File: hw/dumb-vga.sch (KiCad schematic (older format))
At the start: 17 parts, among them IC1 74HC590N, IC2 74HC590N, IC3 74HC590N, U1 A29040C, X1 VGAF

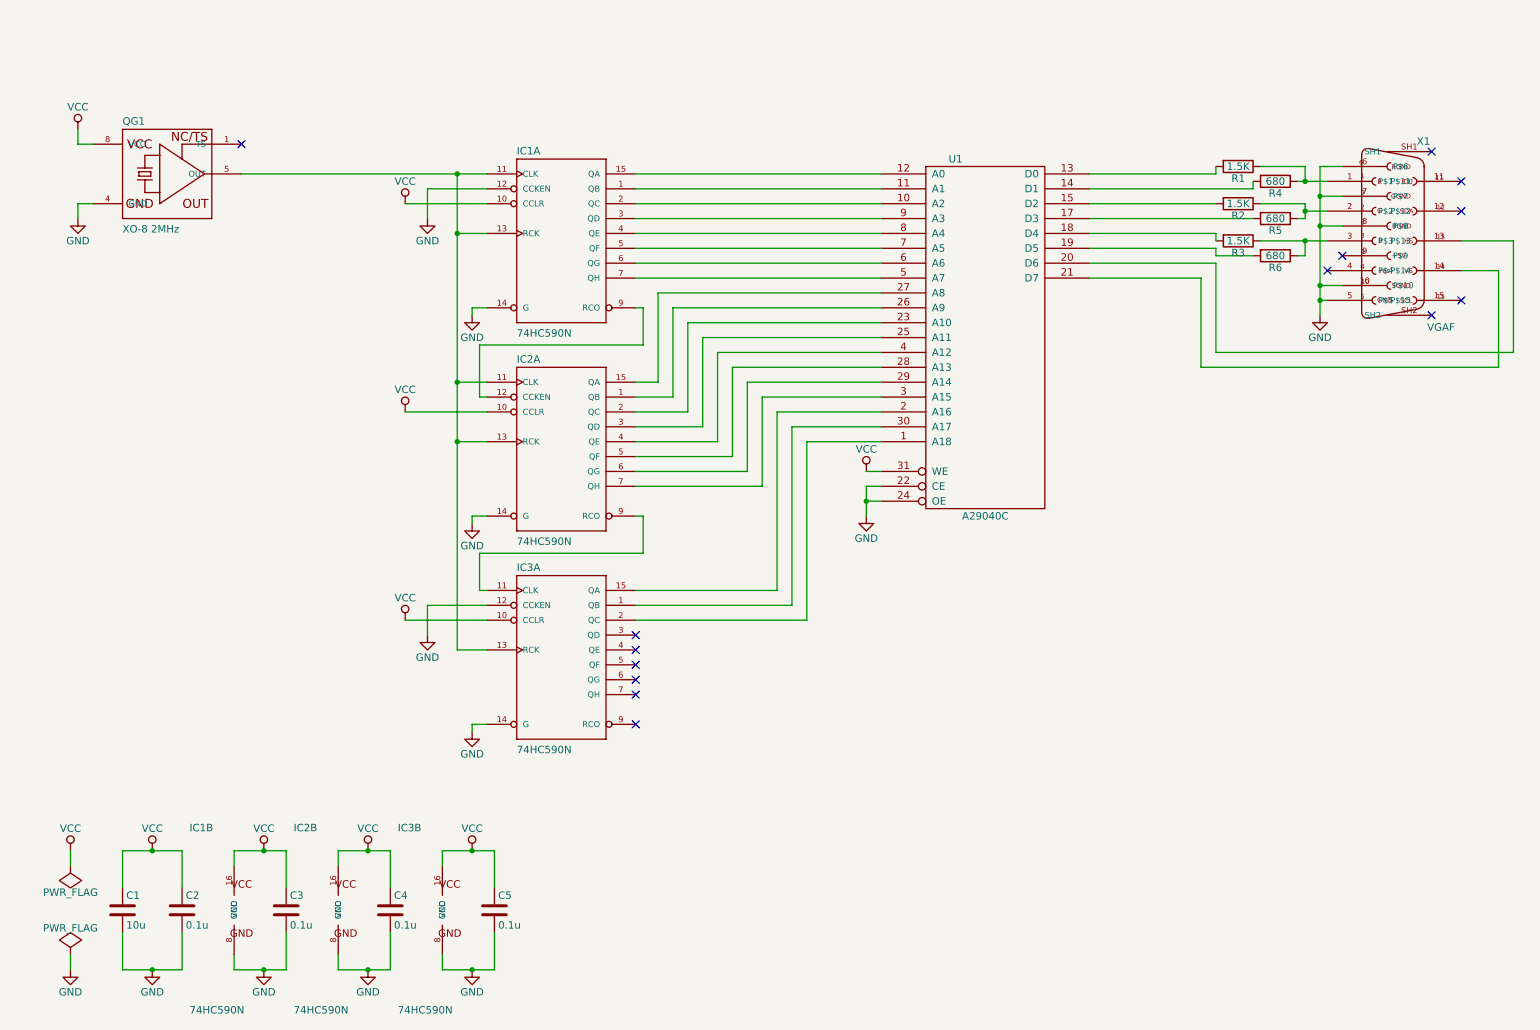
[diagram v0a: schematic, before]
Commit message: v0.1: Added 74574 buffer to eliminate black stripes
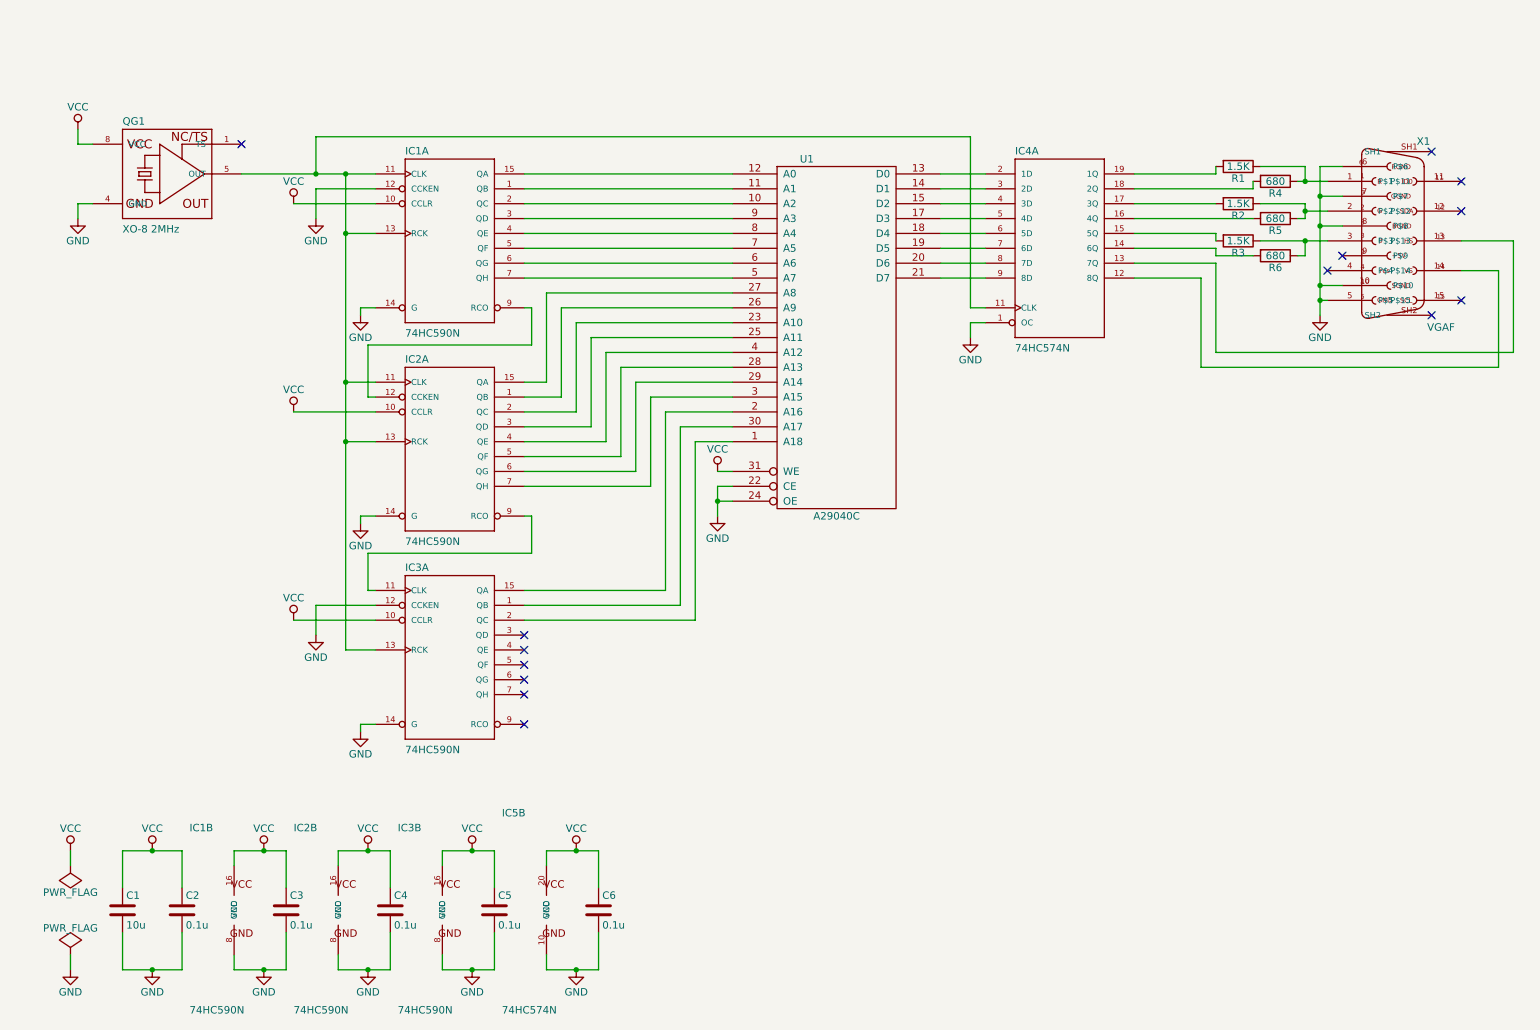
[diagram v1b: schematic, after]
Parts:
- added C6: 0.1u, symbol C
- added IC4, IC5: 74HC574N, 74xx-eu-DIL20, symbol 74HC574N
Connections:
- net GND: now also C6.2, IC4.1 (OC), IC5.10 (GND)
- net VCC: now also C6.1, IC5.20 (VCC)
- net at IC1.11 (CLK), IC1.13 (RCK), IC2.11 (CLK)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: now also IC4.11 (CLK)
- net at R4.2: now also IC4.18 (2Q); no longer U1.14 (D1)
- net at R5.2: now also IC4.16 (4Q); no longer U1.17 (D3)
- net at R6.2: now also IC4.14 (6Q); no longer U1.19 (D5)
- net at R1.2: now also IC4.19 (1Q); no longer U1.13 (D0)
- net at R2.2: now also IC4.17 (3Q); no longer U1.15 (D2)
- net at R3.2: now also IC4.15 (5Q); no longer U1.18 (D4)
- net at X1.13 (P$13): now also IC4.13 (7Q); no longer U1.20 (D6)
- net at X1.14 (P$14): now also IC4.12 (8Q); no longer U1.21 (D7)
- new net: IC4.2 (1D), U1.13 (D0)
- new net: IC4.3 (2D), U1.14 (D1)
- new net: IC4.4 (3D), U1.15 (D2)
- new net: IC4.5 (4D), U1.17 (D3)
- new net: IC4.6 (5D), U1.18 (D4)
- new net: IC4.7 (6D), U1.19 (D5)
- new net: IC4.8 (7D), U1.20 (D6)
- new net: IC4.9 (8D), U1.21 (D7)
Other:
- moved on the sheet: IC1A, IC2A, IC3A, U1

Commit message: v0.2 Upped clock speed, added animation
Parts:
- added C7: 0.1u, symbol C
- added IC6: 74HC04N, 74xx-eu-DIL14, symbol 74HC04N
- QG1: value XO-8 2MHz -> XO-8 16MHz
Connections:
- wire segments 161 -> 168
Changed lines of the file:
@@
 Title "Dumb VGA"
 Date ""
-Rev "v0.1"
+Rev "v0.2"
 Comp ""
 Comment1 "Simple circuit to generate VGA-like signal"
@@
 $EndComp
 $Comp
-L VCC #PWR7
+L VCC #PWR01
 U 1 1 56DA1B02
 P 2150 5950
-F 0 "#PWR7" H 2150 5800 50  0001 C CNN
+F 0 "#PWR01" H 2150 5800 50  0001 C CNN
 F 1 "VCC" H 2150 6100 50  0000 C CNN
 F 2 "" H 2150 5950 50  0000 C CNN
@@
 $EndComp
 $Comp
-L VCC #PWR17
+L VCC #PWR02
 U 1 1 56DA1B3E
 P 2850 5950
-F 0 "#PWR17" H 2850 5800 50  0001 C CNN
+F 0 "#PWR02" H 2850 5800 50  0001 C CNN
 F 1 "VCC" H 2850 6100 50  0000 C CNN
 F 2 "" H 2850 5950 50  0000 C CNN
@@
 $EndComp
 $Comp
-L VCC #PWR19
+L VCC #PWR03
 U 1 1 56DA1B5E
 P 3550 5950
-F 0 "#PWR19" H 3550 5800 50  0001 C CNN
+F 0 "#PWR03" H 3550 5800 50  0001 C CNN
 F 1 "VCC" H 3550 6100 50  0000 C CNN
 F 2 "" H 3550 5950 50  0000 C CNN
@@
 $EndComp
 $Comp
-L GND #PWR20
+L GND #PWR04
 U 1 1 56DA1EF3
 P 3550 6750
-F 0 "#PWR20" H 3550 6500 50  0001 C CNN
+F 0 "#PWR04" H 3550 6500 50  0001 C CNN
 F 1 "GND" H 3550 6600 50  0000 C CNN
 F 2 "" H 3550 6750 50  0000 C CNN
@@
 $EndComp
 $Comp
-L GND #PWR18
+L GND #PWR05
 U 1 1 56DA1FE2
 P 2850 6750
-F 0 "#PWR18" H 2850 6500 50  0001 C CNN
+F 0 "#PWR05" H 2850 6500 50  0001 C CNN
 F 1 "GND" H 2850 6600 50  0000 C CNN
 F 2 "" H 2850 6750 50  0000 C CNN
@@
 $EndComp
 $Comp
-L GND #PWR8
+L GND #PWR06
 U 1 1 56DA2011
 P 2150 6750
-F 0 "#PWR8" H 2150 6500 50  0001 C CNN
+F 0 "#PWR06" H 2150 6500 50  0001 C CNN
 F 1 "GND" H 2150 6600 50  0000 C CNN
 F 2 "" H 2150 6750 50  0000 C CNN
@@
 NoConn ~ 3900 4700
 NoConn ~ 3900 4800
-NoConn ~ 3900 4900
 $Comp
 L XO-8 QG1
@@
 P 1500 1400
 F 0 "QG1" H 1200 1725 50  0000 L BNN
-F 1 "XO-8 2MHz" H 1200 1000 50  0000 L BNN
+F 1 "XO-8 16MHz" H 1200 1000 50  0000 L BNN
 F 2 "crystal-DIL08S" H 1500 1550 50  0001 C CNN
 F 3 "" H 1500 1400 60  0000 C CNN
@@
 $EndComp
 $Comp
-L VCC #PWR3
+L VCC #PWR07
 U 1 1 56DA29D7
 P 900 1100
-F 0 "#PWR3" H 900 950 50  0001 C CNN
+F 0 "#PWR07" H 900 950 50  0001 C CNN
 F 1 "VCC" H 900 1250 50  0000 C CNN
 F 2 "" H 900 1100 50  0000 C CNN
@@
 $EndComp
 $Comp
-L GND #PWR4
+L GND #PWR08
 U 1 1 56DA2A09
 P 900 1700
-F 0 "#PWR4" H 900 1450 50  0001 C CNN
+F 0 "#PWR08" H 900 1450 50  0001 C CNN
 F 1 "GND" H 900 1550 50  0000 C CNN
 F 2 "" H 900 1700 50  0000 C CNN
@@
 NoConn ~ 2000 1200
 $Comp
-L GND #PWR24
+L GND #PWR09
 U 1 1 56DA2E52
 P 5200 3700
-F 0 "#PWR24" H 5200 3450 50  0001 C CNN
+F 0 "#PWR09" H 5200 3450 50  0001 C CNN
 F 1 "GND" H 5200 3550 50  0000 C CNN
 F 2 "" H 5200 3700 50  0000 C CNN
@@
 $EndComp
 $Comp
-L VCC #PWR23
+L VCC #PWR010
 U 1 1 56DA2FBD
 P 5200 3400
-F 0 "#PWR23" H 5200 3250 50  0001 C CNN
+F 0 "#PWR010" H 5200 3250 50  0001 C CNN
 F 1 "VCC" H 5200 3550 50  0000 C CNN
 F 2 "" H 5200 3400 50  0000 C CNN
@@
 $EndComp
 $Comp
-L GND #PWR14
+L GND #PWR011
 U 1 1 56DA30CB
 P 2800 2350
-F 0 "#PWR14" H 2800 2100 50  0001 C CNN
+F 0 "#PWR011" H 2800 2100 50  0001 C CNN
 F 1 "GND" H 2800 2200 50  0000 C CNN
 F 2 "" H 2800 2350 50  0000 C CNN
@@
 $EndComp
 $Comp
-L GND #PWR15
+L GND #PWR012
 U 1 1 56DA30FD
 P 2800 3750
-F 0 "#PWR15" H 2800 3500 50  0001 C CNN
+F 0 "#PWR012" H 2800 3500 50  0001 C CNN
 F 1 "GND" H 2800 3600 50  0000 C CNN
 F 2 "" H 2800 3750 50  0000 C CNN
@@
 $EndComp
 $Comp
-L GND #PWR16
+L GND #PWR013
 U 1 1 56DA31B1
 P 2800 5150
-F 0 "#PWR16" H 2800 4900 50  0001 C CNN
+F 0 "#PWR013" H 2800 4900 50  0001 C CNN
 F 1 "GND" H 2800 5000 50  0000 C CNN
 F 2 "" H 2800 5150 50  0000 C CNN
@@
 $EndComp
 $Comp
-L GND #PWR12
+L GND #PWR014
 U 1 1 56DA3E4A
 P 2500 1700
-F 0 "#PWR12" H 2500 1450 50  0001 C CNN
+F 0 "#PWR014" H 2500 1450 50  0001 C CNN
 F 1 "GND" H 2500 1550 50  0000 C CNN
 F 2 "" H 2500 1700 50  0000 C CNN
@@
 $EndComp
 $Comp
-L GND #PWR13
+L GND #PWR015
 U 1 1 56DA3EAE
 P 2500 4500
-F 0 "#PWR13" H 2500 4250 50  0001 C CNN
+F 0 "#PWR015" H 2500 4250 50  0001 C CNN
 F 1 "GND" H 2500 4350 50  0000 C CNN
 F 2 "" H 2500 4500 50  0000 C CNN
@@
 $EndComp
 $Comp
-L VCC #PWR9
+L VCC #PWR016
 U 1 1 56DA4042
 P 2350 1600
-F 0 "#PWR9" H 2350 1450 50  0001 C CNN
+F 0 "#PWR016" H 2350 1450 50  0001 C CNN
 F 1 "VCC" H 2350 1750 50  0000 C CNN
 F 2 "" H 2350 1600 50  0000 C CNN
@@
 $EndComp
 $Comp
-L VCC #PWR10
+L VCC #PWR017
 U 1 1 56DA4074
 P 2350 3000
-F 0 "#PWR10" H 2350 2850 50  0001 C CNN
+F 0 "#PWR017" H 2350 2850 50  0001 C CNN
 F 1 "VCC" H 2350 3150 50  0000 C CNN
 F 2 "" H 2350 3000 50  0000 C CNN
@@
 $EndComp
 $Comp
-L VCC #PWR11
+L VCC #PWR018
 U 1 1 56DA40E7
 P 2350 4400
-F 0 "#PWR11" H 2350 4250 50  0001 C CNN
+F 0 "#PWR018" H 2350 4250 50  0001 C CNN
 F 1 "VCC" H 2350 4550 50  0000 C CNN
 F 2 "" H 2350 4400 50  0000 C CNN
@@
 $EndComp
 $Comp
-L VCC #PWR5
+L VCC #PWR019
 U 1 1 56DA442B
 P 1400 5950
-F 0 "#PWR5" H 1400 5800 50  0001 C CNN
+F 0 "#PWR019" H 1400 5800 50  0001 C CNN
 F 1 "VCC" H 1400 6100 50  0000 C CNN
 F 2 "" H 1400 5950 50  0000 C CNN
@@
 $EndComp
 $Comp
-L GND #PWR6
+L GND #PWR020
 U 1 1 56DA445D
 P 1400 6750
-F 0 "#PWR6" H 1400 6500 50  0001 C CNN
+F 0 "#PWR020" H 1400 6500 50  0001 C CNN
 F 1 "GND" H 1400 6600 50  0000 C CNN
 F 2 "" H 1400 6750 50  0000 C CNN
@@
 $EndComp
 $Comp
-L GND #PWR26
+L GND #PWR021
 U 1 1 56DA4B82
 P 9250 2350
-F 0 "#PWR26" H 9250 2100 50  0001 C CNN
+F 0 "#PWR021" H 9250 2100 50  0001 C CNN
 F 1 "GND" H 9250 2200 50  0000 C CNN
 F 2 "" H 9250 2350 50  0000 C CNN
@@
 	5300 3200 5050 3200
 Wire Wire Line
-	5050 3200 5050 4400
-Wire Wire Line
-	5050 4400 3900 4400
+	5050 3200 5050 4900
 Wire Wire Line
 	900  1100 900  1200
@@
 	8450 2700 8450 2100
 $Comp
-L PWR_FLAG #FLG1
+L PWR_FLAG #FLG022
 U 1 1 56DA6820
 P 850 6050
-F 0 "#FLG1" H 850 6145 50  0001 C CNN
+F 0 "#FLG022" H 850 6145 50  0001 C CNN
 F 1 "PWR_FLAG" H 850 6230 50  0000 C CNN
 F 2 "" H 850 6050 50  0000 C CNN
@@
 $EndComp
 $Comp
-L VCC #PWR1
+L VCC #PWR023
 U 1 1 56DA68DE
 P 850 5950
-F 0 "#PWR1" H 850 5800 50  0001 C CNN
+F 0 "#PWR023" H 850 5800 50  0001 C CNN
 F 1 "VCC" H 850 6100 50  0000 C CNN
 F 2 "" H 850 5950 50  0000 C CNN
@@
 	850  5950 850  6050
 $Comp
-L GND #PWR2
+L GND #PWR024
 U 1 1 56DA6AC0
 P 850 6750
-F 0 "#PWR2" H 850 6500 50  0001 C CNN
+F 0 "#PWR024" H 850 6500 50  0001 C CNN
 F 1 "GND" H 850 6600 50  0000 C CNN
 F 2 "" H 850 6750 50  0000 C CNN
@@
 $EndComp
 $Comp
-L PWR_FLAG #FLG2
+L PWR_FLAG #FLG025
 U 1 1 56DA6B84
 P 850 6650
-F 0 "#FLG2" H 850 6745 50  0001 C CNN
+F 0 "#FLG025" H 850 6745 50  0001 C CNN
 F 1 "PWR_FLAG" H 850 6830 50  0000 C CNN
 F 2 "" H 850 6650 50  0000 C CNN
@@
 	8450 2100 8000 2100
 $Comp
-L GND #PWR25
+L GND #PWR026
 U 1 1 56DACC69
 P 6900 2500
-F 0 "#PWR25" H 6900 2250 50  0001 C CNN
+F 0 "#PWR026" H 6900 2250 50  0001 C CNN
 F 1 "GND" H 6900 2350 50  0000 C CNN
 F 2 "" H 6900 2500 50  0000 C CNN
@@
 	6900 2400 6900 2500
 Wire Wire Line
-	7000 2300 6900 2300
-Wire Wire Line
-	6900 2300 6900 1150
-Wire Wire Line
-	6900 1150 2500 1150
-Wire Wire Line
-	2500 1150 2500 1400
+	6900 2300 7000 2300
+Wire Wire Line
+	2500 900  2500 1400
 Connection ~ 2500 1400
 $Comp
@@
 $EndComp
 $Comp
-L VCC #PWR21
+L VCC #PWR027
 U 1 1 56DAD35F
 P 4250 5950
-F 0 "#PWR21" H 4250 5800 50  0001 C CNN
+F 0 "#PWR027" H 4250 5800 50  0001 C CNN
 F 1 "VCC" H 4250 6100 50  0000 C CNN
 F 2 "" H 4250 5950 50  0000 C CNN
@@
 $EndComp
 $Comp
-L GND #PWR22
+L GND #PWR028
 U 1 1 56DAD3AF
 P 4250 6750
-F 0 "#PWR22" H 4250 6500 50  0001 C CNN
+F 0 "#PWR028" H 4250 6500 50  0001 C CNN
 F 1 "GND" H 4250 6600 50  0000 C CNN
 F 2 "" H 4250 6750 50  0000 C CNN
@@
 	4400 5950 4400 6200
 Connection ~ 4250 5950
+$Comp
+L 74HC04N IC6
+U 1 1 56DBE569
+P 6000 900
+F 0 "IC6" H 6100 1025 50  0000 L BNN
+F 1 "74HC04N" H 6100 700 50  0000 L BNN
+F 2 "74xx-eu-DIL14" H 6000 1050 50  0001 C CNN
+F 3 "" H 6000 900 60  0000 C CNN
+	1    6000 900
+	1    0    0    -1
+$EndComp
+Wire Wire Line
+	6400 900  6900 900
+Wire Wire Line
+	6900 900  6900 2300
+Wire Wire Line
+	5600 900  2500 900
+$Comp
+L 74HC04N IC6
+U 7 1 56DBE990
+P 4750 6350
+F 0 "IC6" H 4850 6475 50  0000 L BNN
+F 1 "74HC04N" H 4850 6150 50  0000 L BNN
+F 2 "74xx-eu-DIL14" H 4750 6500 50  0001 C CNN
+F 3 "" H 4750 6350 60  0000 C CNN
+	7    4750 6350
+	1    0    0    -1
+$EndComp
+$Comp
+L C C7
+U 1 1 56DBEA02
+P 5100 6350
+F 0 "C7" H 5125 6450 50  0000 L CNN
+F 1 "0.1u" H 5125 6250 50  0000 L CNN
+F 2 "" H 5138 6200 50  0000 C CNN
+F 3 "" H 5100 6350 50  0000 C CNN
+	1    5100 6350
+	1    0    0    -1
+$EndComp
+$Comp
+L VCC #PWR029
+U 1 1 56DBEA71
+P 4950 5950
+F 0 "#PWR029" H 4950 5800 50  0001 C CNN
+F 1 "VCC" H 4950 6100 50  0000 C CNN
+F 2 "" H 4950 5950 50  0000 C CNN
+F 3 "" H 4950 5950 50  0000 C CNN
+	1    4950 5950
+	1    0    0    -1
+$EndComp
+$Comp
+L GND #PWR030
+U 1 1 56DBEACA
+P 4950 6750
+F 0 "#PWR030" H 4950 6500 50  0001 C CNN
+F 1 "GND" H 4950 6600 50  0000 C CNN
+F 2 "" H 4950 6750 50  0000 C CNN
+F 3 "" H 4950 6750 50  0000 C CNN
+	1    4950 6750
+	1    0    0    -1
+$EndComp
+Wire Wire Line
+	4750 6650 4750 6750
+Wire Wire Line
+	4750 6750 5100 6750
+Wire Wire Line
+	5100 6750 5100 6500
+Connection ~ 4950 6750
+Wire Wire Line
+	5100 5950 5100 6200
+Wire Wire Line
+	4750 5950 5100 5950
+Wire Wire Line
+	4750 6050 4750 5950
+Connection ~ 4950 5950
+Wire Wire Line
+	5050 4900 3900 4900
+NoConn ~ 3900 4400
 $EndSCHEMATC
